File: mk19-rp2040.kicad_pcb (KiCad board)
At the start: 2 copper layers, 130 x 85 mm, 134 parts, among them J1 USB_C_Receptacle_USB2.0, J10 Conn_01x02, J11 Conn_01x03_Socket, J12 USB_C_Receptacle_USB2.0, J13 USB_C_Receptacle_USB2.0, J2 Conn_01x03_Socket, J3 Conn_01x02_Socket, J4 Conn_01x06_Socket, J5 Conn_01x02, J7 Conn_01x02_Socket, J8 Conn_01x02_Socket, J9 Conn_01x02_Socket, T1 Conn_01x01_Socket, T10 Conn_01x01_Socket, T11 Conn_01x01_Socket, T12 Conn_01x01_Socket, T13 Conn_01x01_Socket, T14 Conn_01x01_Socket, T15 Conn_01x01_Socket, T2 Conn_01x01_Socket, T3 Conn_01x01_Socket, T5 Conn_01x01_Socket, T6 Conn_01x01_Socket, T7 Conn_01x01_Socket, T9 Conn_01x01_Socket, U1 RP2040, U10 1N4148W_C81598, U11 1N4148W_C81598, U12 1N4148W_C81598, U13 1N4148W_C81598, U14 1N4148W_C81598, U15 1N4148W_C81598, U2 USBLC6-2P6, U3 XC6210B332MR-G, U4 USBLC6-2P6, U5 W25Q128JVS, U6 8_01A0_008200, U7 8_01A0_008200, U8 USBLC6-2P6, U9 1N4148W_C81598, Y1 Crystal_GND24

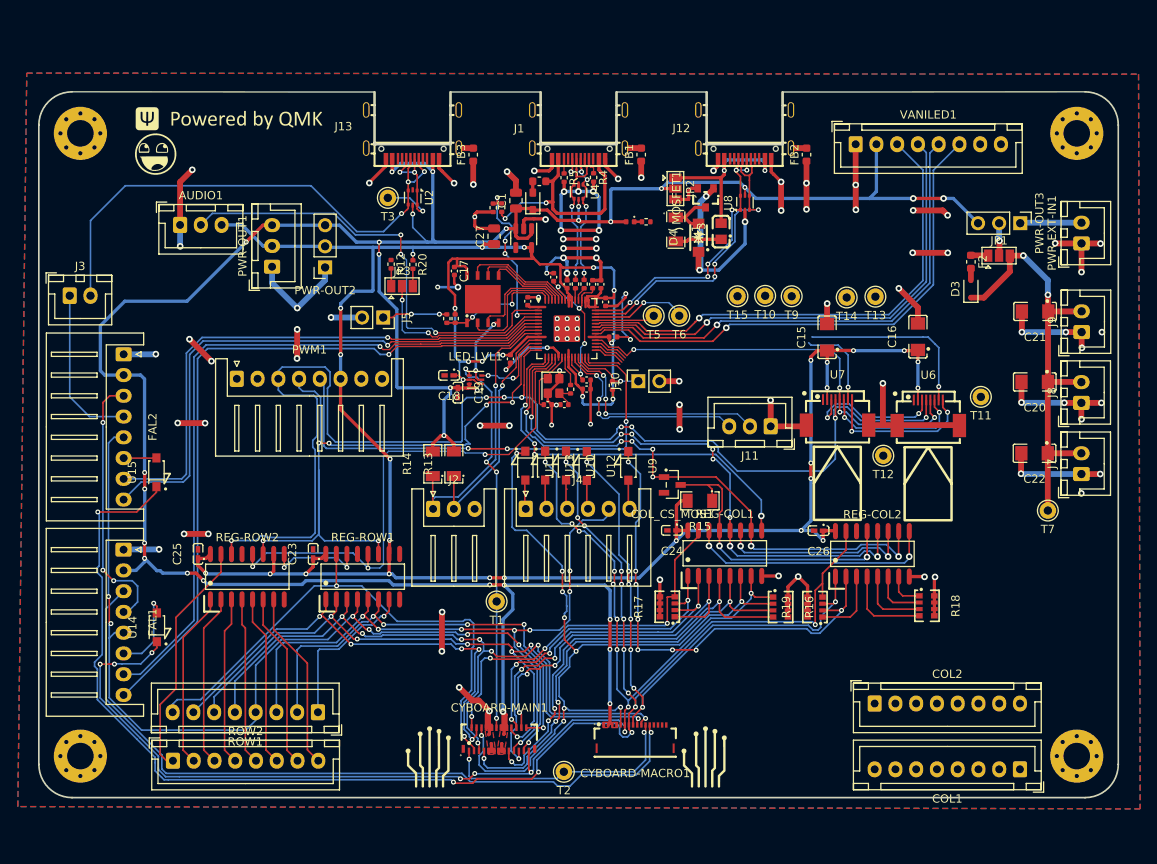
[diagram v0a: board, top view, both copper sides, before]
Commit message: drc passing, everything hooked up
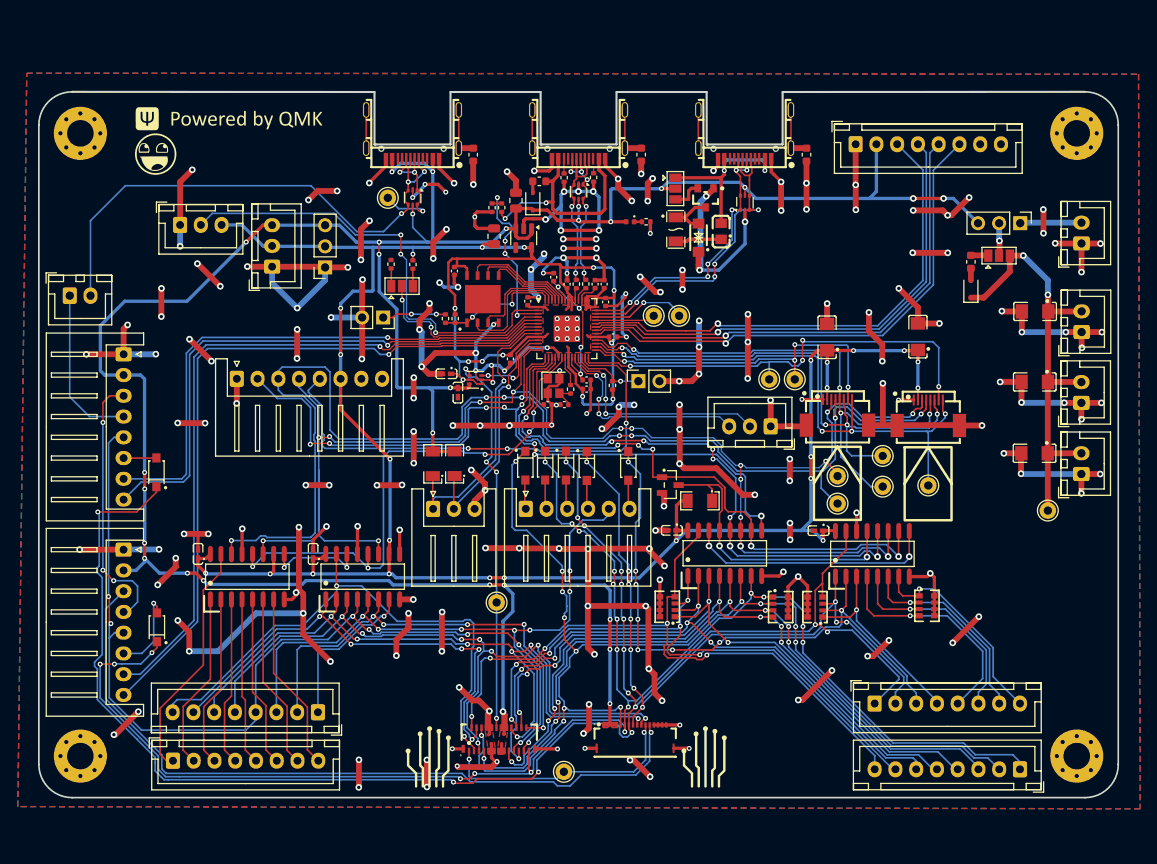
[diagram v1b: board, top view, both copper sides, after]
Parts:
- moved LOGO3 125.8 mm to (135.5, 64.5)
- moved T14 24.8 mm to (224.1, 97.7)
- moved T15 24.8 mm to (224.1, 94.4)
- moved T13 22.9 mm to (229.5, 95.7)
- moved T11 12.4 mm to (235.0, 95.5)
- moved T10 10.7 mm to (218.9, 82.8)
- moved T9 10.4 mm to (215.9, 82.8)
- moved C5 0.39 mm to (196.0, 71.3)
- moved C18 0.36 mm to (177.0, 82.1)
- moved C6 0.30 mm to (194.9, 71.3)
- moved COL_CS_MOS1 0.24 mm to (204.0, 95.5)
- moved R7 0.20 mm to (193.8, 71.3)
- moved R3 0.16 mm to (176.9, 75.4)
- moved R11 0.14 mm to (182.5, 62.1)
- moved T1 0.12 mm to (183.0, 109.6)
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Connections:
- C10 pad 1: unconnected-(C10-Pad1) -> +3V3
- C10 pad 2: unconnected-(C10-Pad2) -> GND
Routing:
- net GND: track 354.8 -> 746.3 mm, vias 104 -> 230
- net SPI1_CLK: track 123.3 -> 182.3 mm, vias 10 -> 16
- net SPI1_MISO: track 47.7 -> 91.6 mm, vias 4 -> 8
- net col7: track 152.8 -> 195.7 mm, vias 16 -> 19
- net LCD_DC: track 21.8 -> 64.5 mm, vias 2 -> 4
- net LCD_BL: track 22.7 -> 64.9 mm, vias 2 -> 4
- net col6: track 96.1 -> 135.6 mm, vias 10 -> 13
- net col1: track 37.8 -> 75.8 mm, vias 4 -> 6
- net col3: track 42.8 -> 80.1 mm, vias 4 -> 5
- net col0: track 46.1 -> 82.7 mm, vias 4 -> 5
- net col2: track 44.6 -> 80.8 mm, vias 4 -> 6
- net col5: track 54.2 -> 89.4 mm, vias 4 -> 7
- net col4: track 51.2 -> 83.9 mm, vias 4 -> 7
- net LCD1_CS: track 26.6 -> 54.9 mm, vias 1 -> 4
- net LCD2_CS: track 14.5 -> 42.0 mm, vias 1 -> 4
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- added copper zone on F.Cu, net +3V3

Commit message: more changes, pcba insights coming next
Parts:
- moved T7 31.1 mm to (237.5, 69.8)
- moved J7 19.8 mm to (239.3, 80.2)
- moved C22 18.5 mm to (244.7, 73.5)
- moved C20 12.8 mm to (244.7, 70.7)
- moved J8 9.03 mm to (246.2, 80.2)
- moved C21 7.41 mm to (244.7, 67.9)
- moved J9 3.59 mm to (253.1, 73.5)
- moved JP1 3.39 mm to (243.5, 64.5)
- moved PWR-EXT-IN1 3.38 mm to (252.3, 63.2)
- moved F2 3.35 mm to (240.1, 65.3)
- moved D3 3.08 mm to (240.1, 68.8)
- moved PWR-OUT3 2.97 mm to (246.1, 61.0)
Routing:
- net GND: track 746.3 -> 743.3 mm, vias 230 -> 224
- net +5V: track 334.1 -> 332.9 mm
- net Net-(PWR-EXT-IN1-Pin_2): track 7.40 -> 6.39 mm
- net LED_5V: track 53.6 -> 53.4 mm, vias 2 -> 3

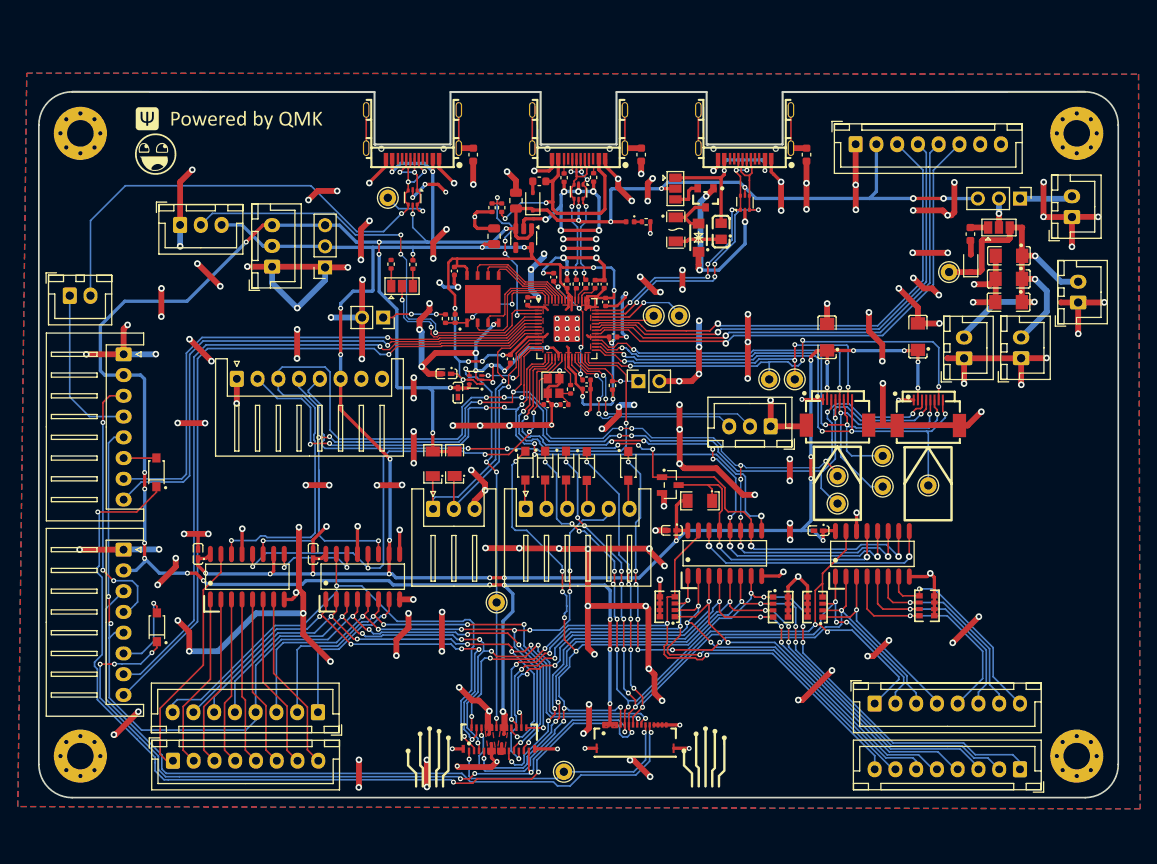
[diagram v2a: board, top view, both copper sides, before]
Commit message: reworking some of this, copy paste introduced errors whee
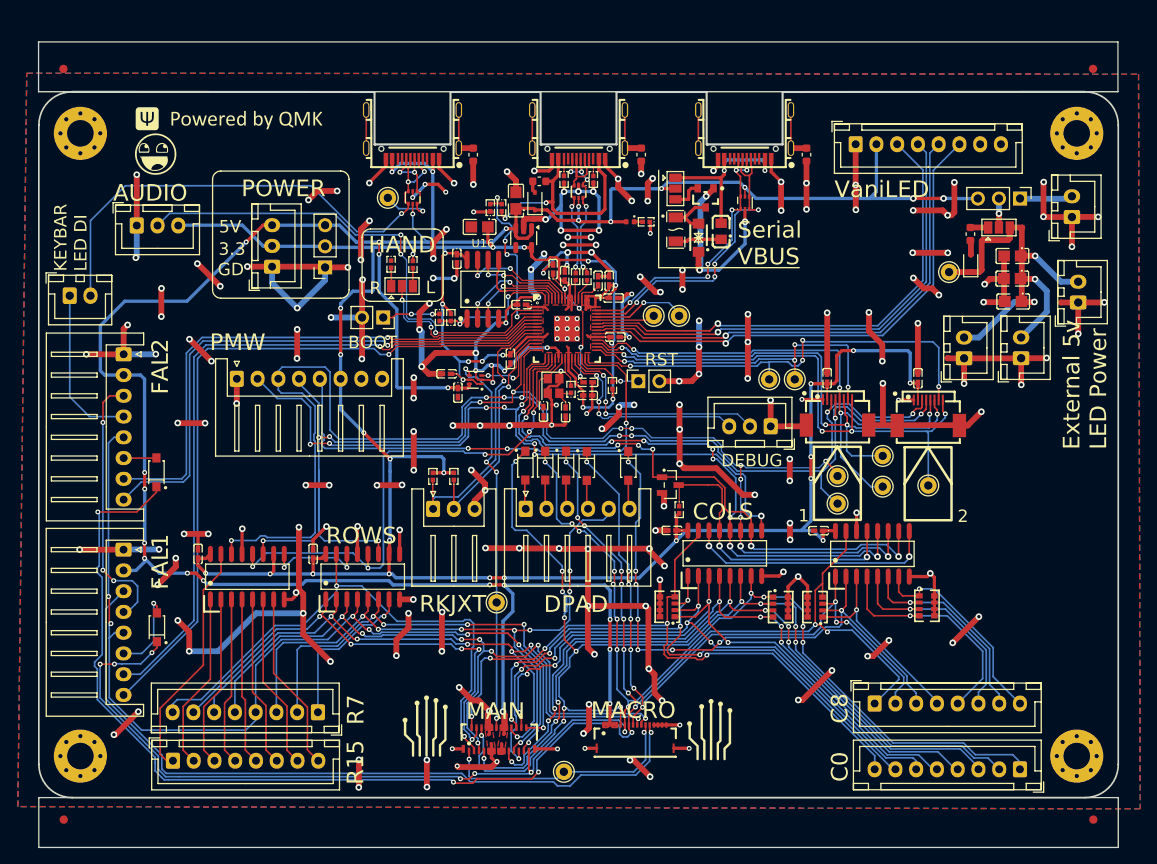
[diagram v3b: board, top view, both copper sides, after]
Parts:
- removed C20, C21, C22: CL31B105KBHNNNE, ct-kicad:C1206
- removed U5: W25Q128JVS, drawings:W25Q128JVPIQ
- added C2: 10u, ct-kicad:C0805, F.Cu at (245.2, 67.9)
- added C28: 10u, ct-kicad:C0805, F.Cu at (245.1, 70.6)
- added C29: 10u, ct-kicad:C0805, F.Cu at (245.2, 73.4)
- added FID1: Fiducial, Fiducial:Fiducial_1mm_Mask2mm, F.Cu at (130.9, 45.4)
- added FID2: Fiducial, Fiducial:Fiducial_1mm_Mask2mm, F.Cu at (254.9, 45.4)
- added FID3: Fiducial, Fiducial:Fiducial_1mm_Mask2mm, F.Cu at (254.9, 135.8)
- added FID4: Fiducial, Fiducial:Fiducial_1mm_Mask2mm, F.Cu at (130.9, 135.8)
- added U16: W25Q128JVSIQTR, ct-kicad:SOIC-8_L5.3-W5.3-P1.27-LS8.0-BL, F.Cu at (181.4, 71.9)
- C1, C27: footprint Capacitor_SMD:C_0805_2012Metric -> ct-kicad:C0805
- C10, C11, C12, C13, C14, C7, C8, C9: value 100n -> 100nf; footprint Capacitor_SMD:C_0402_1005Metric -> ct-kicad:C0402
- C15, C16: value CL31B105KBHNNNE -> 1u; footprint ct-kicad:C1206 -> ct-kicad:C0402
- C17, C5, C6: value 1µ -> 1u; footprint Capacitor_SMD:C_0402_1005Metric -> ct-kicad:C0402
- C18, C19, C23, C24, C25, C26: value 100nF -> 100nf
- C3, C4: footprint Capacitor_SMD:C_0402_1005Metric -> ct-kicad:C0402
- R1, R10, R11, R12, R2, R20, R3, R4, R5, R6, R7, R8, R9: footprint Resistor_SMD:R_0402_1005Metric -> ct-kicad:R0402
- R13, R14: value 4.7k -> 5.1k; footprint ct-kicad:R1206 -> ct-kicad:R0402
- R15: value 1206W4F1002T5E -> 10k; footprint ct-kicad:R1206 -> ct-kicad:R0402
- U1: footprint 0xLib_Package_DFN_QFN:QFN-56-1EP_7x7mm_P0.4mm_EP3.2x3.2mm -> ct-kicad:LQFN-56_L7.0-W7.0-P0.4-EP
- U2, U4, U8: footprint Package_TO_SOT_SMD:SOT-666 -> ct-kicad:SOT-666-6_L1.6-W1.2-P0.50-LS1.6-BL
- moved LOGO3 100.8 mm to (215.8, 125.5)
- moved AUDIO1 5.22 mm to (139.7, 64.2)
- moved C16 5.01 mm to (233.8, 82.6)
- moved C15 4.93 mm to (222.8, 82.6)
- moved LOGO7 3.73 mm to (174.6, 124.1)
- moved LOGO6 3.36 mm to (208.9, 124.5)
- moved R15 2.71 mm to (205.0, 98.5), turned to -90 degrees
- moved C27 2.08 mm to (181.0, 64.4), turned to 180 degrees
- moved R13 1.52 mm to (177.9, 94.4)
- moved R14 1.51 mm to (175.4, 94.4)
- moved C17 1.51 mm to (178.2, 68.2)
- moved C11 1.07 mm to (197.1, 73.0), turned to 0 degrees
- moved C10 1.02 mm to (191.2, 70.3)
- moved C3 0.98 mm to (188.7, 86.6), turned to -90 degrees
- moved C7 0.97 mm to (189.8, 69.5)
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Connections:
- R13 pad 2: +5V -> +3V3
- R14 pad 2: +5V -> +3V3
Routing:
- net +5V: track 332.9 -> 322.4 mm, vias 28 -> 27
- net GND: track 743.3 -> 752.4 mm, vias 224 -> 223
- net +3V3: track 342.3 -> 349.1 mm, vias 34 -> 33
- net AUDIO: track 55.1 -> 60.3 mm
- net /QSPI_D0: track 9.32 -> 13.6 mm, vias 0 -> 2
- net /QSPI_D1: track 14.3 -> 10.7 mm
- net /QSPI_~{CS}: track 14.9 -> 17.5 mm
- net +1V1: track 21.9 -> 23.5 mm
- net /QSPI_D3: track 13.3 -> 14.9 mm, vias 0 -> 2
- net PMW_CS: track 61.4 -> 60.3 mm
- net Net-(U1-USB_DM): track 1.86 -> 2.81 mm
- net Net-(U1-USB_DP): track 1.48 -> 2.42 mm
- net USB-MAIN_+: track 19.7 -> 18.8 mm
- net /VBUS_DET: track 20.8 -> 21.7 mm
- net USB-MAIN_-: track 19.0 -> 18.3 mm
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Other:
- board size 130 x 85 mm -> 130 x 97 mm
- board text added: "1"
- board text added: "2"
- board text added: "3.3"
- board text added: "5V"
- board text added: "AUDIO"
- board text added: "BOOT"
- board text added: "C0"
- board text added: "C8"
- board text added: "COLS"
- board text added: "DEBUG"
- board text added: "DPAD"
- board text added: "External 5v LED Power"
- board text added: "FAL1"
- board text added: "FAL2"
- board text added: "GD"
- board text added: "HAND"
- board text added: "KEYBAR LED DI"
- board text added: "L"
- board text added: "MACRO"
- board text added: "MAIN"
- board text added: "PMW"
- board text added: "POWER"
- board text added: "R"
- board text added: "R15"
- board text added: "R7"
- board text added: "RKJXT"
- board text added: "ROWS"
- board text added: "RST"
- board text added: "Serial VBUS"
- board text added: "VaniLED"

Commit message: drc passing, bom generating correctly, silkscreen v1
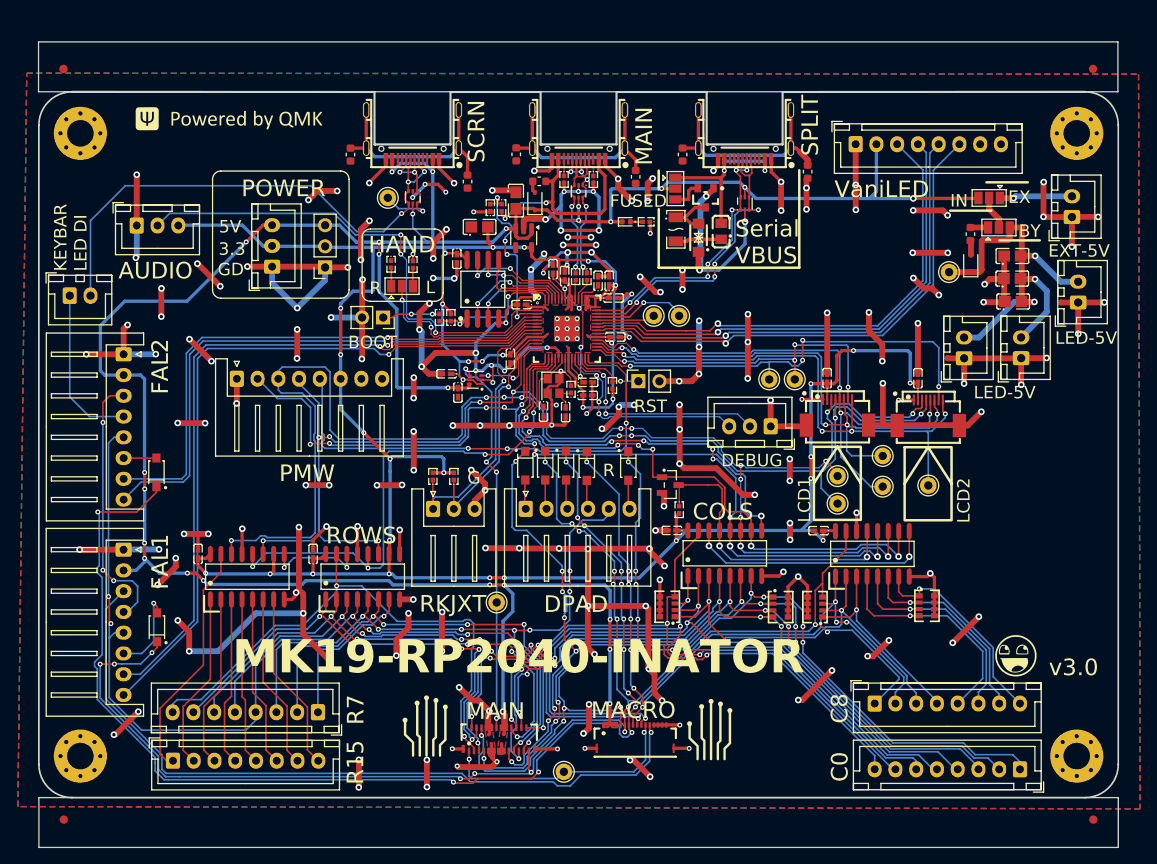
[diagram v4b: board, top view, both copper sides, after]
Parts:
- removed PWR-OUT3: Conn_01x03_Socket, Connector_PinHeader_2.54mm:PinHeader_1x03_P2.54mm_Vertical
- removed U2, U4, U8: USBLC6-2P6, ct-kicad:SOT-666-6_L1.6-W1.2-P0.50-LS1.6-BL
- added D5: USBLC6-2P6_C2827693, ct-kicad:SOT-666-6_L1.6-W1.2-P0.50-LS1.6-BL, F.Cu at (212.9, 61.6)
- added D6: USBLC6-2P6_C2827693, ct-kicad:SOT-666-6_L1.6-W1.2-P0.50-LS1.6-BL, F.Cu at (172.9, 60.8)
- added D7: USBLC6-2P6_C2827693, ct-kicad:SOT-666-6_L1.6-W1.2-P0.50-LS1.6-BL, F.Cu at (192.9, 60.1)
- added FB4: FerriteBead_Small, Inductor_SMD:L_0603_1608Metric, F.Cu at (185.4, 55.7)
- added FB5: FerriteBead_Small, Inductor_SMD:L_0603_1608Metric, F.Cu at (205.4, 55.7)
- added FB6: FerriteBead_Small, Inductor_SMD:L_0603_1608Metric, F.Cu at (165.4, 55.7)
- added JP4: SolderJumper_3_Open, Jumper:SolderJumper-3_P1.3mm_Open_Pad1.0x1.5mm, F.Cu at (242.4, 60.9)
- moved LOGO1 120.0 mm to (245.7, 115.9)
- moved LOGO4 119.9 mm to (245.6, 116.0)
- moved FB3 3.31 mm to (179.5, 58.9)
- moved FB1 2.75 mm to (199.8, 58.4)
- moved FB2 2.05 mm to (220.5, 57.8)
- moved D1 0.46 mm to (198.7, 63.8)
- turned C1 to -90 degrees
- turned C2 to 0 degrees
- turned C27 to 0 degrees
- turned C28 to 0 degrees
- turned C29 to 0 degrees
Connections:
- C1 pad 1: +5V -> GND
- C1 pad 2: GND -> +5V
- C2 pad 1: LED_5V -> GND
- C2 pad 2: GND -> LED_5V
- C27 pad 1: +3V3 -> GND
- C27 pad 2: GND -> +3V3
- C28 pad 1: LED_5V -> GND
- C28 pad 2: GND -> LED_5V
- C29 pad 1: LED_5V -> GND
- C29 pad 2: GND -> LED_5V
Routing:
- net Net-(J13-SHIELD): track 10.9 -> 26.8 mm
- net Net-(J1-SHIELD): track 11.2 -> 26.5 mm
- net Net-(J12-SHIELD): track 11.1 -> 26.2 mm
- net GND: track 752.4 -> 743.4 mm, vias 223 -> 220
- net Net-(JP4-A): track 6.39 -> 8.78 mm, vias 0 -> 1
- net Net-(JP1-C): track 3.50 -> 4.05 mm, vias 1 -> 0
- net +5V: track 322.4 -> 322.7 mm, vias 27 -> 26
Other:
- board text added: "BY"
- board text added: "EX"
- board text added: "EXT-5V"
- board text added: "FUSED"
- board text added: "G"
- board text added: "IN"
- board text added: "LCD1"
- board text added: "LCD2"
- board text added: "LED-5V"
- board text added: "MK19-RP2040-INATOR"
- board text added: "SCRN"
- board text added: "SPLIT"
- board text added: "v3.0"
- board text removed: "1"
- board text removed: "2"
- board text removed: "External 5v LED Power"

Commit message: getting manufacturing bits ready
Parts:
- added H5: MountingHole, MountingHole:MountingHole_2.1mm, F.Cu at (142.4, 45.0)
- added H6: MountingHole, MountingHole:MountingHole_2.1mm, F.Cu at (240.7, 44.7)
- added H7: MountingHole, MountingHole:MountingHole_2.1mm, F.Cu at (144.0, 135.9)
- added H8: MountingHole, MountingHole:MountingHole_2.1mm, F.Cu at (240.1, 136.4)
- moved C13 0.62 mm to (197.9, 77.7)
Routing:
- net GND: track 743.4 -> 741.0 mm, vias 220 -> 219
- net /QSPI_~{CS}: track 17.5 -> 15.8 mm
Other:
- board size 130 x 97 mm -> 130 x 100 mm
- board text added: "V-CUT"
